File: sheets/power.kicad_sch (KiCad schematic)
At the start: 63 parts, among them Q11 C1815, Q12 A1015, Q13 A1442, T1 COIL, U11 74LS05, U12 74LS06, U28 PC4741, U29 PC4741, U33 74AS04, U37 LM2576T-5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

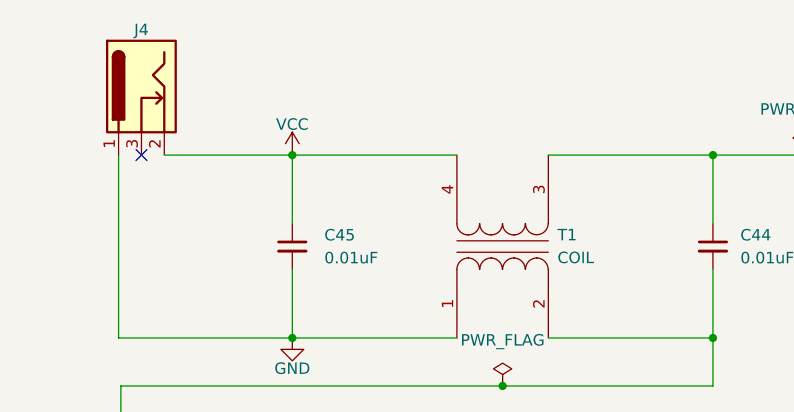
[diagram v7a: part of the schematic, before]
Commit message: Changed Power input on DC Jack to be +9v instead of VCC Zero errors on PCB
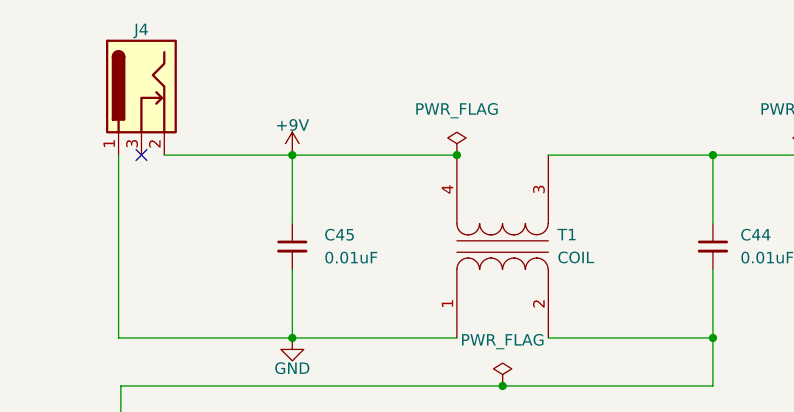
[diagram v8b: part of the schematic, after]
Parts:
- U33, U8, U80: footprint (none) -> Package_DIP:DIP-14_W7.62mm
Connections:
- net VCC: no longer C45.1, J4.2, T1.4 (SB)
- new net +9V: C45.1, J4.2, T1.4 (SB)
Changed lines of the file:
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@@
   (junction (at 59.055 127) (diameter 0) (color 0 0 0 0)
+  )
+  (junction (at 64.77 29.972) (diameter 0) (color 0 0 0 0)
   )
   (junction (at 51.562 65.786) (diameter 0) (color 0 0 0 0)
@@
       (effects (font (size 1.27 1.27)))
     )
-    (property "Footprint" "" (at 342.9 238.76 0)
+    (property "Footprint" "Package_DIP:DIP-14_W7.62mm" (at 342.9 238.76 0)
       (effects (font (size 1.27 1.27)) hide)
     )
@@
       (effects (font (size 1.27 1.27)))
     )
-    (property "Footprint" "" (at 30.48 218.44 0)
+    (property "Footprint" "Package_DIP:DIP-14_W7.62mm" (at 30.48 218.44 0)
       (effects (font (size 1.27 1.27)) hide)
     )
@@
     )
   )
+  (symbol (lib_id "power:PWR_FLAG") (at 64.77 29.972 0) (unit 1)
+    (in_bom yes) (on_board yes) (dnp no) (fields_autoplaced)
+    (property "Reference" "#FLG01" (at 64.77 28.067 0)
+      (effects (font (size 1.27 1.27)) hide)
+    )
+    (property "Value" "PWR_FLAG" (at 64.77 24.892 0)
+      (effects (font (size 1.27 1.27)))
+    )
+    (property "Footprint" "" (at 64.77 29.972 0)
+      (effects (font (size 1.27 1.27)) hide)
+    )
+    (property "Datasheet" "~" (at 64.77 29.972 0)
+      (effects (font (size 1.27 1.27)) hide)
+    )
+    (pin "1")
+    (instances
+      (project "NeoGeoAES3_5"
+        (path "/e226ecbc-35ef-48b6-a608-5f12ffad334e/395516b4-de87-4f49-9253-15d185c97222"
+          (reference "#FLG01") (unit 1)
+        )
+      )
+    )
+  )
   (symbol (lib_id "power:VCC") (at 108.966 108.458 180) (unit 1)
     (in_bom yes) (on_board yes) (dnp no)
@@
       (effects (font (size 1.27 1.27)))
     )
-    (property "Footprint" "" (at 30.48 203.2 0)
+    (property "Footprint" "Package_DIP:DIP-14_W7.62mm" (at 30.48 203.2 0)
       (effects (font (size 1.27 1.27)) hide)
     )
@@
     )
   )
-  (symbol (lib_id "power:VCC") (at 46.482 29.972 0) (unit 1)
-    (in_bom yes) (on_board yes) (dnp no)
-    (property "Reference" "#PWR0276" (at 46.482 33.782 0)
-      (effects (font (size 1.27 1.27)) hide)
-    )
-    (property "Value" "VCC" (at 46.482 26.5684 0)
-      (effects (font (size 1.27 1.27)))
-    )
-    (property "Footprint" "" (at 46.482 29.972 0)
-      (effects (font (size 1.27 1.27)) hide)
-    )
-    (property "Datasheet" "" (at 46.482 29.972 0)
-      (effects (font (size 1.27 1.27)) hide)
-    )
-    (pin "1")
-    (instances
-      (project "NeoGeoAES3_5"
-        (path "/e226ecbc-35ef-48b6-a608-5f12ffad334e/395516b4-de87-4f49-9253-15d185c97222"
-          (reference "#PWR0276") (unit 1)
-        )
-      )
-    )
-  )
   (symbol (lib_id "power:VCC") (at 23.368 246.38 0) (unit 1)
     (in_bom yes) (on_board yes) (dnp no)
@@
     )
   )
+  (symbol (lib_id "power:+9V") (at 46.482 29.972 0) (unit 1)
+    (in_bom yes) (on_board yes) (dnp no) (fields_autoplaced)
+    (property "Reference" "#PWR01" (at 46.482 33.782 0)
+      (effects (font (size 1.27 1.27)) hide)
+    )
+    (property "Value" "+9V" (at 46.482 26.67 0)
+      (effects (font (size 1.27 1.27)))
+    )
+    (property "Footprint" "" (at 46.482 29.972 0)
+      (effects (font (size 1.27 1.27)) hide)
+    )
+    (property "Datasheet" "" (at 46.482 29.972 0)
+      (effects (font (size 1.27 1.27)) hide)
+    )
+    (pin "1")
+    (instances
+      (project "NeoGeoAES3_5"
+        (path "/e226ecbc-35ef-48b6-a608-5f12ffad334e/395516b4-de87-4f49-9253-15d185c97222"
+          (reference "#PWR01") (unit 1)
+        )
+      )
+    )
+  )
   (symbol (lib_id "power:GND") (at 111.506 29.972 0) (unit 1)
     (in_bom yes) (on_board yes) (dnp no)
@@
       (effects (font (size 1.27 1.27)))
     )
-    (property "Footprint" "" (at 314.96 238.76 0)
+    (property "Footprint" "Package_DIP:DIP-14_W7.62mm" (at 314.96 238.76 0)
       (effects (font (size 1.27 1.27)) hide)
     )
@@
       (effects (font (size 1.27 1.27)))
     )
-    (property "Footprint" "" (at 30.48 187.96 0)
-      (effects (font (size 1.27 1.27)) hide)
-    )
+    (property "Footprint" "Package_DIP:DIP-14_W7.62mm" (at 30.48 187.96 0)
+      (effects (font (size 1.27 1.27)) hide)
+    )
